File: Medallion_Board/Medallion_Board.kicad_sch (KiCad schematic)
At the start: 3 parts, among them U1 ESP32-S3, U2 MIA-M10Q-00B, U3 ICM-20948

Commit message: Schematic in a good place. IMU, GNSS, LoRa, lipo charging and usb, and neopixels all in.
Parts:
- removed U1: ESP32-S3, Package_DFN_QFN:QFN-56-1EP_7x7mm_P0.4mm_EP4x4mm, symbol MCU_Espressif:ESP32-S3
- removed U2: MIA-M10Q-00B, MIA-M10Q-00B:BGA53C50P9X9_450X450X100, symbol MIA-M10Q-00B:MIA-M10Q-00B
- removed U3: ICM-20948, ICM-20948:QFN40P300X300X105-24N, symbol ICM-20948:ICM-20948
- added C1, C14, C17, C2, C7, C9: 10uF, Capacitor_SMD:C_0805_2012Metric, symbol Adafruit ESP32-S3 8MB No PSRAM-eagle-import:CAP_CERAMIC0805-NOOUTLINE
- added C10, C4, C5: 1uF, Capacitor_SMD:C_0603_1608Metric, symbol Adafruit ESP32-S3 8MB No PSRAM-eagle-import:CAP_CERAMIC0603_NO
- added C11, C6, C8: 10µF, Capacitor_SMD:C_0805_2012Metric, symbol Adafruit ESP32-S3 8MB No PSRAM-eagle-import:CAP_CERAMIC0805-NOOUTLINE
- added C12: 0.1µF, Capacitor_SMD:C_0805_2012Metric, symbol Adafruit ESP32-S3 8MB No PSRAM-eagle-import:CAP_CERAMIC0805-NOOUTLINE
- added C13: 0.1uF, Capacitor_SMD:C_0603_1608Metric, symbol Adafruit ESP32-S3 8MB No PSRAM-eagle-import:CAP_CERAMIC0603_NO
- added C15: 0.1uF, Capacitor_SMD:C_0805_2012Metric, symbol Adafruit ESP32-S3 8MB No PSRAM-eagle-import:CAP_CERAMIC0805-NOOUTLINE
- added C16: 47pF, Capacitor_SMD:C_0805_2012Metric, symbol Adafruit ESP32-S3 8MB No PSRAM-eagle-import:CAP_CERAMIC0805-NOOUTLINE
- added C18: 100nF, Capacitor_SMD:C_0603_1608Metric, symbol Adafruit ESP32-S3 8MB No PSRAM-eagle-import:CAP_CERAMIC0603_NO
- added C3: KW-5R5C104-R, KW-5R5C104-R:CAPPRD500W60D1000H3150, symbol XH414HG-IV01E:XH414HG-IV01E
- added CHG2: ORANGE, LED_SMD:LED_0805_2012Metric, symbol Adafruit ESP32-S3 8MB No PSRAM-eagle-import:LED0603_NOOUTLINE
- added D3: RED, LED_SMD:LED_0603_1608Metric, symbol Adafruit ESP32-S3 8MB No PSRAM-eagle-import:LED0603_NOOUTLINE
- added D4: MBR540, Diode_SMD:D_SOD-123, symbol Adafruit ESP32-S3 8MB No PSRAM-eagle-import:DIODE-SCHOTTKYSOD-123
- added FL1, FL2: BLM15EG121SN1D, BLM15EG121SN1D:BEADC1005X55N, symbol BLM15EG121SN1D:BLM15EG121SN1D
- added J1: RYLR998, Connector_PinHeader_2.54mm:PinHeader_1x05_P2.54mm_Vertical, symbol Connector_Generic:Conn_01x05
- added LED1, LED2, LED3, LED4, LED5, LED6, LED7, LED8, LED9: WS2812B_SK6805_2020, LED_SMD:LED_WS2812B-2020_PLCC4_2.0x2.0mm, symbol Adafruit ESP32-S3 8MB No PSRAM-eagle-import:WS2812B_SK6805_1515
- added Q3: DMG3415U, DMG3415U-7:SOT95P240X105-3N, symbol Adafruit ESP32-S3 8MB No PSRAM-eagle-import:MOSFET-P
- added R1, R10, R11, R13, R6, R9: 5.1K, Resistor_SMD:R_0603_1608Metric, symbol Adafruit ESP32-S3 8MB No PSRAM-eagle-import:RESISTOR_0603_NOOUT
- added R12, R7: 100K, Resistor_SMD:R_0603_1608Metric, symbol Adafruit ESP32-S3 8MB No PSRAM-eagle-import:RESISTOR_0603_NOOUT
- added R17: 1Meg, Resistor_SMD:R_0603_1608Metric, symbol Adafruit ESP32-S3 8MB No PSRAM-eagle-import:RESISTOR_0603_NOOUT
- added R18: 10K, Resistor_SMD:R_0603_1608Metric, symbol Adafruit ESP32-S3 8MB No PSRAM-eagle-import:RESISTOR_0603_NOOUT
- added R3: 10K, Resistor_SMD:R_0603_1608Metric, symbol Adafruit ESP32-S3 8MB No PSRAM-eagle-import:RESISTOR_4PACK
- added R8: 1K, Resistor_SMD:R_0603_1608Metric, symbol Adafruit ESP32-S3 8MB No PSRAM-eagle-import:RESISTOR_0603_NOOUT
- added SW1, SW2: KMR2, Button_Switch_SMD:SW_Push_1P1T-SH_NO_CK_KMR2xxG, symbol Adafruit ESP32-S3 8MB No PSRAM-eagle-import:SWITCH_TACT_SMT4.6X2.8
- added U1: LC86LICMD, LC86LICMD:MODULE_LC86LICMD, symbol LC86LICMD:LC86LICMD
- added U2: AP2112/RT9080-3.3, RT9080-33GJ5:SOT94P280X100-5N, symbol Adafruit ESP32-S3 8MB No PSRAM-eagle-import:VREG_SOT23-5
- added U3: ESP32-S3-MINI-1-N8, ESP32-S3-MINI-1-N8:XCVR_ESP32-S3-MINI-1-N8, symbol ESP32-S3-MINI-1-N8:ESP32-S3-MINI-1-N8
- added U4: BNO085, BNO085:IC_BNO085, symbol BNO085:BNO085
- added U5: MCP73831T-2ACI_OT, MCP73831T-2ACI_OT:SOT95P280X145-5N, symbol MCP73831T-2ACI_OT:MCP73831T-2ACI_OT
- added U6: MAX17048G_T10, MAX17048G_T10:SON50P200X200X80-9N, symbol MAX17048G_T10:MAX17048G_T10
- added X1: JSTPH, Connector_JST:JST_PH_S2B-PH-SM4-TB_1x02-1MP_P2.00mm_Horizontal, symbol Adafruit ESP32-S3 8MB No PSRAM-eagle-import:CON_JST_PH_2PIN_MT_BATT
- added X2: USB4085-GF-A, USB4085-GF-A:GCT_USB4085-GF-A_REVB, symbol USB4085-GF-A:USB4085-GF-A
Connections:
- net GND: now also C1.2, C10.2, C11.2, C12.2, C13.1, C14.2, C15.2, C16.2, C17.2, C18.2, C2.2, C3.2, C4.2, C5.2, C6.2, C7.2, C8.2, C9.2, D3.1, FL2.1, FL2.2, J1.5 (GND), LED1.4 (GND), LED2.4 (GND), LED3.4 (GND), LED4.4 (GND), LED5.4 (GND), LED6.4 (GND), LED7.4 (GND), LED8.4 (GND), LED9.4 (GND), R11.1, R12.1, R13.1, R17.1, R9.1, SW1.1, SW2.1, U1.12 (GND), U1.3 (GND), U2.2 (GND), U3.1 (GND), U3.2 (GND), U3.42 (GND), U3.43 (GND), U3.46 (GND), U3.47 (GND), U3.48 (GND), U3.49 (GND), U3.50 (GND), U3.51 (GND), U3.52 (GND), U3.53 (GND), U3.54 (GND), U3.55 (GND), U3.56 (GND), U3.57 (GND), U3.58 (GND), U3.59 (GND), U3.60 (GND), U3.61 (GND), U3.61_1 (GND), U3.61_2 (GND), U3.61_3 (GND), U3.61_4 (GND), U3.61_5 (GND), U3.61_6 (GND), U3.61_7 (GND), U3.61_8 (GND), U3.62 (GND), U3.63 (GND), U3.64 (GND), U3.65 (GND), U4.2 (GND), U4.25 (GNDIO), U4.5 (PS1), U4.6 (PS0/WAKE), U5.2 (VSS), U6.1 (CTG), U6.4 (GND), U6.6 (QSTRT), U6.9 (EP), X1.1, X2.A1 (GND), X2.A12 (GND), X2.B1 (GND), X2.B12 (GND)
- new net: C18.1, U4.9 (CAP)
- new net: R9.2, U5.5 (PROG)
- new net: R18.1, U4.4 (~{BOOT})
- new net: LED5.3 (DO), LED6.1 (DI)
- new net: LED6.3 (DO), LED7.1 (DI)
- new net: C12.1, U2.4 (P4)
- new net: LED7.3 (DO), LED8.1 (DI)
- new net: LED8.3 (DO), LED9.1 (DI)
- new net: R7.1, U2.3 (EN)
- new net: CHG2.1, R6.1
- new net: R6.2, U5.1 (STAT)
- new net: LED2.3 (DO), LED3.1 (DI)
- new net: LED3.3 (DO), LED4.1 (DI)
- new net: U4.1 (RESV_NC), U4.12 (RESV_NC), U4.13 (RESV_NC), U4.21 (RESV_NC), U4.22 (RESV_NC), U4.23 (RESV_NC), U4.24 (RESV_NC), U4.7 (RESV_NC), U4.8 (RESV_NC)
- new net: C14.1, C15.1, C16.1, FL1.2, J1.1 (VDD)
- new net: R13.2, X2.B5 (CC2)
- new net: D3.2, R10.2
- new net: LED1.3 (DO), LED2.1 (DI)
- new net: R11.2, X2.A5 (CC1)
- new net: C3.1, R8.2, U1.5 (V_BCKP)
- new net: LED4.3 (DO), LED5.1 (DI)
- new net: X2.S1 (SHELL), X2.S2 (SHELL), X2.S3 (SHELL), X2.S4 (SHELL)
- new net +3.3V: C17.1, FL1.1, LED1.2 (VDD), LED2.2 (VDD), LED3.2 (VDD), LED4.2 (VDD), LED5.2 (VDD), LED6.2 (VDD), LED7.2 (VDD), LED8.2 (VDD), LED9.2 (VDD), R3.1 (2), R3.2
- new net 3.3V: C1.1, C10.1, C2.1, C7.1, C8.1, C9.1, R1.2, R18.2, R8.1, U1.4 (VCC), U2.5 (OUT), U3.3 (3V3), U4.28 (VDDIO), U4.3 (VDD)
- new net BNO_NINT: U4.14 (~{H_INT})
- new net BNO_NRST: U4.11 (~{RST})
- new net BOOT0: SW1.2, U3.4 (IO0)
- new net D+: U3.24 (IO20), X2.A6 (DP1)
- new net D-: U3.23 (IO19), X2.B6 (DP2)
- new net D13: R10.1, U3.17 (IO13)
- new net GPS_ANT_ACTIVE: U1.8 (AADET_N), U3.14 (IO10)
- new net GPS_RESET: U1.10 (~{RESET}), U3.13 (IO9)
- new net GPS_WAKEUP: U1.7 (WAKE_UP), U3.12 (IO8)
- new net I2C_PWR: U3.11 (IO7)
- new net IO34_DBLTAP: C5.1, R17.2, U3.29 (IO34)
- new net LORA_NRST: J1.2 (~{RST})
- new net LOW_BATT: U3.9 (IO5), U6.5 (~{ALERT})
- new net NEOPIX: LED1.1 (DI), U3.28 (IO33)
- new net RESET: C4.1, R1.1, SW2.2, U3.45 (EN)
- new net RXD0: U1.2 (TXD), U3.33 (IO37)
- new net RXD1: J1.4 (TXD), U3.35 (IO39)
- new net SCL: R3.1, U3.8 (IO4), U4.19 (H_SCL/SCK/RX), U6.7 (SCL)
- new net SDA: R3.2 (1), U3.7 (IO3), U4.20 (H_SDA/H_MISO/TX), U6.8 (SDA)
- new net TXD0: U1.1 (RXD), U3.32 (IO36)
- new net TXD1: J1.3 (RXD), U3.34 (IO38)
- new net VBAT: C11.1, C13.2, Q3.3 (D), U5.3 (VBAT), U6.2 (CELL), U6.3 (VDD), X1.2
- new net VBUS: CHG2.2, D4.1, Q3.1 (G), R12.2, U5.4 (VDD), X2.A4 (VBUS), X2.A9 (VBUS), X2.B4 (VBUS), X2.B9 (VBUS)
- new net VHI: C6.1, D4.2, Q3.2 (S), R7.2, U2.1 (IN)
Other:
- note added: "1.0K = 1000mA"
- note added: "10K = 100mA"
- note added: "2.0K = 500mA"
- note added: "5.0K = 200mA"
- note added: "Bulk decoupling"
- note added: "CONTROLLER"
- note added: "FUEL GAUGE"
- note added: "GPS"
- note added: "High-frequency filter"
- note added: "I2C SUPPORT"
- note added: "IMU SENSOR"
- note added: "LED"
- note added: "LIPO CHARGING AND REPORTING"
- note added: "LORA RADIO"
- note added: "NEOPIXEL"
- note added: "POWER AND FILTERING"
- note added: "Place as near to ESP32 power rail as possible"
- note added: "USB AND PROGRAMMING BUTTONS"

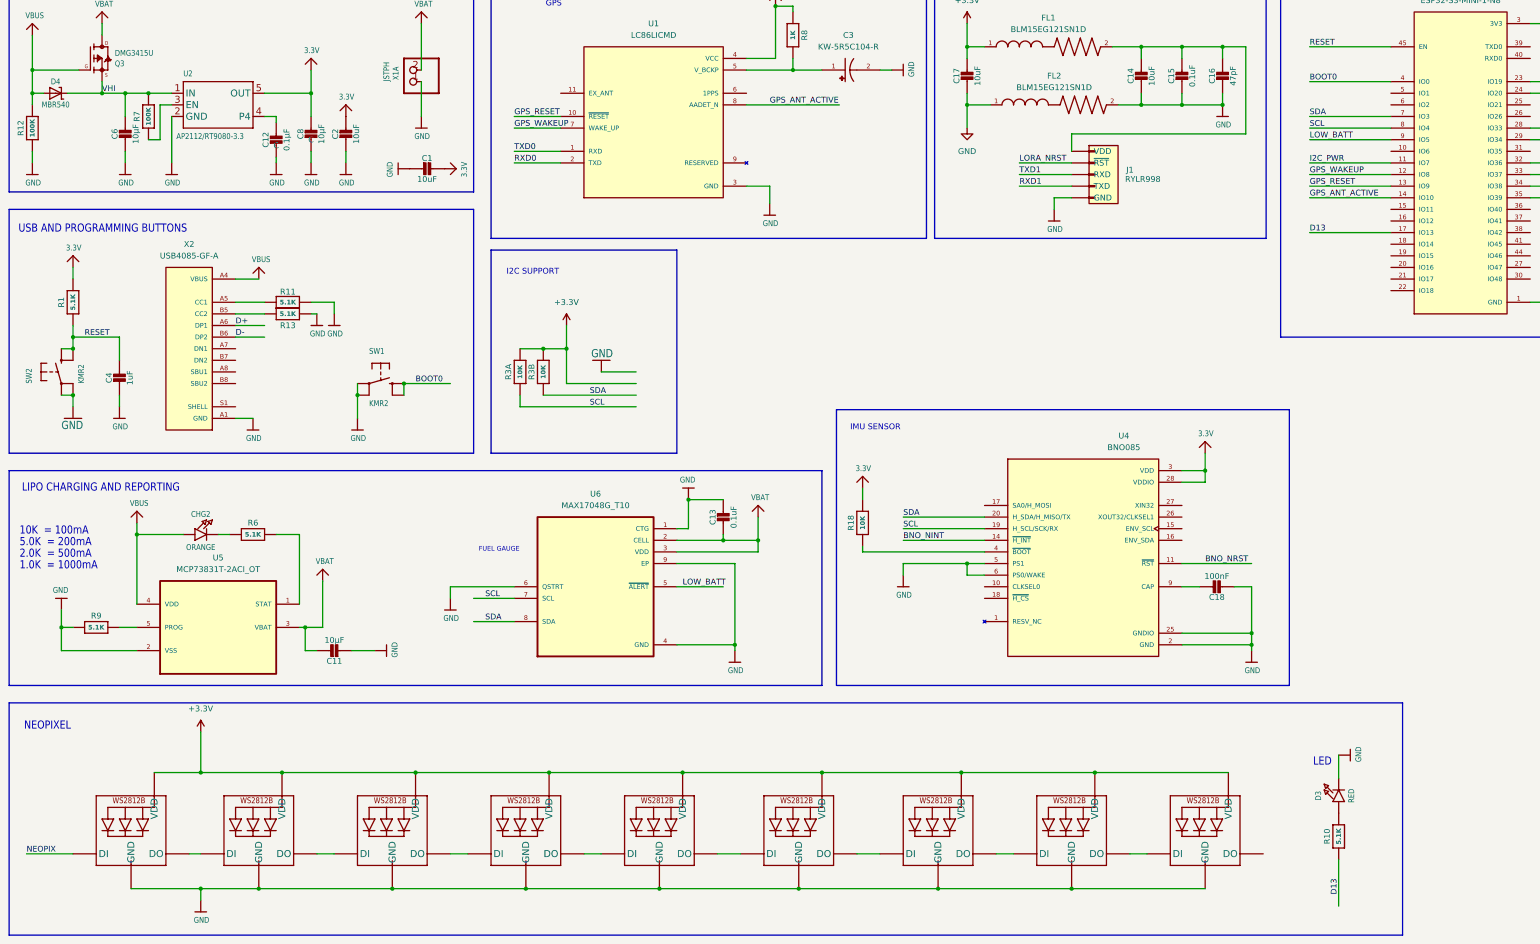
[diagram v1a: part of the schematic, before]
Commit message: Double checked capacitor values and footprints
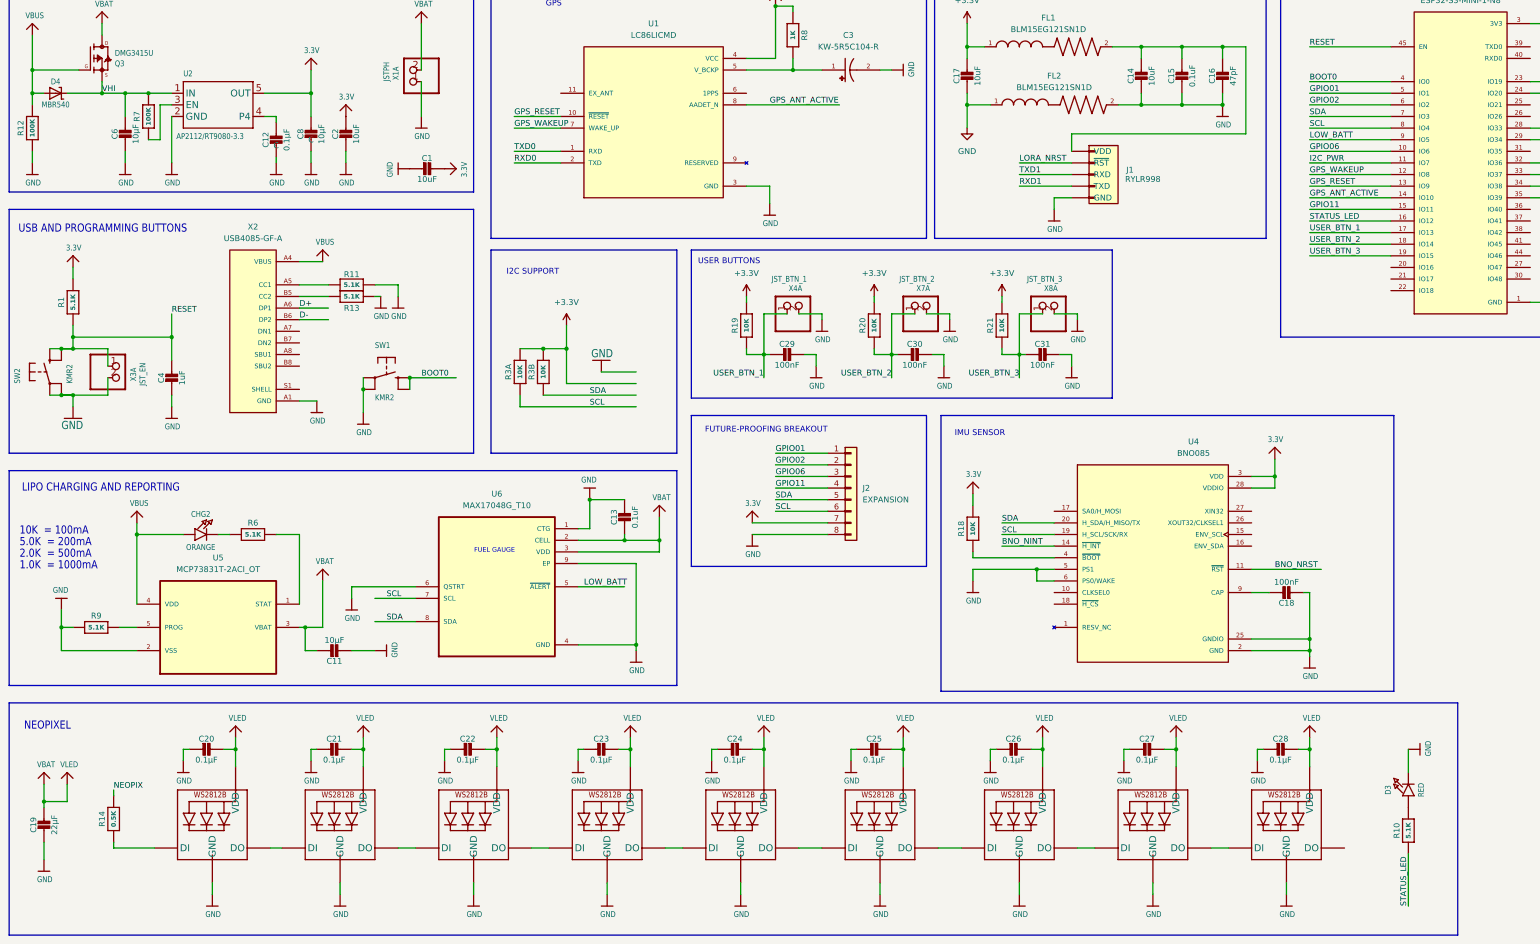
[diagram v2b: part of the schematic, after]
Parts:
- added C19: 22µF, Capacitor_SMD:C_0805_2012Metric, symbol Adafruit ESP32-S3 8MB No PSRAM-eagle-import:CAP_CERAMIC0805-NOOUTLINE
- added C20, C21, C22, C23, C24, C25, C26, C27, C28: 0.1µF, Capacitor_SMD:C_0603_1608Metric, symbol Adafruit ESP32-S3 8MB No PSRAM-eagle-import:CAP_CERAMIC0805-NOOUTLINE
- added C29, C30, C31: 100nF, Capacitor_SMD:C_0603_1608Metric, symbol Adafruit ESP32-S3 8MB No PSRAM-eagle-import:CAP_CERAMIC0603_NO
- added J2: EXPANSION, Connector_PinHeader_2.54mm:PinHeader_1x08_P2.54mm_Vertical, symbol Connector_Generic:Conn_01x08
- added R14: 0.5K, Resistor_SMD:R_0603_1608Metric, symbol Adafruit ESP32-S3 8MB No PSRAM-eagle-import:RESISTOR_0603_NOOUT
- added R19, R20, R21: 10K, Resistor_SMD:R_0603_1608Metric, symbol Adafruit ESP32-S3 8MB No PSRAM-eagle-import:RESISTOR_0603_NOOUT
- added X3: JST_EN, Connector_JST:JST_PH_S2B-PH-SM4-TB_1x02-1MP_P2.00mm_Horizontal, symbol Adafruit ESP32-S3 8MB No PSRAM-eagle-import:CON_JST_PH_2PIN_MT_BATT
- added X4: JST_BTN_1, Connector_JST:JST_PH_S2B-PH-SM4-TB_1x02-1MP_P2.00mm_Horizontal, symbol Adafruit ESP32-S3 8MB No PSRAM-eagle-import:CON_JST_PH_2PIN_MT_BATT
- added X7: JST_BTN_2, Connector_JST:JST_PH_S2B-PH-SM4-TB_1x02-1MP_P2.00mm_Horizontal, symbol Adafruit ESP32-S3 8MB No PSRAM-eagle-import:CON_JST_PH_2PIN_MT_BATT
- added X8: JST_BTN_3, Connector_JST:JST_PH_S2B-PH-SM4-TB_1x02-1MP_P2.00mm_Horizontal, symbol Adafruit ESP32-S3 8MB No PSRAM-eagle-import:CON_JST_PH_2PIN_MT_BATT
- C12, C15, C16: footprint Capacitor_SMD:C_0805_2012Metric -> Capacitor_SMD:C_0402_1005Metric
- C13: footprint Capacitor_SMD:C_0603_1608Metric -> Capacitor_SMD:C_0402_1005Metric
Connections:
- net +3.3V: now also R19.2, R20.2, R21.2; no longer LED1.2 (VDD), LED2.2 (VDD), LED3.2 (VDD), LED4.2 (VDD), LED5.2 (VDD), LED6.2 (VDD), LED7.2 (VDD), LED8.2 (VDD), LED9.2 (VDD)
- net 3.3V: now also J2.7 (Pin_7)
- net GND: now also C19.2, C20.2, C21.2, C22.2, C23.2, C24.2, C25.2, C26.2, C27.2, C28.2, C29.1, C30.1, C31.1, J2.8 (Pin_8), X3.2, X4.2, X7.2, X8.2
- net NEOPIX: now also R14.2; no longer LED1.1 (DI)
- net RESET: now also X3.1
- net SCL: now also J2.6 (Pin_6)
- net SDA: now also J2.5 (Pin_5)
- net VBAT: now also LED1.2 (VDD), LED2.2 (VDD), LED3.2 (VDD), LED4.2 (VDD), LED5.2 (VDD), LED6.2 (VDD), LED7.2 (VDD), LED8.2 (VDD), LED9.2 (VDD), C19.1, C20.1, C21.1, C22.1, C23.1, C24.1, C25.1, C26.1, C27.1, C28.1
- net GPIO06: now reaches U3.10 (IO6)
- net GPIO06: now also J2.3 (Pin_3)
- net GPIO11: now reaches U3.15 (IO11)
- net GPIO11: now also J2.4 (Pin_4)
- net STATUS_LED: now reaches U3.16 (IO12)
- net STATUS_LED: now also R10.1
- net USER_BTN_2: now reaches U3.18 (IO14)
- net USER_BTN_2: now also C30.2, R20.1, X7.1
- net USER_BTN_3: now reaches U3.19 (IO15)
- net USER_BTN_3: now also C31.2, R21.1, X8.1
- net GPIO01: now reaches U3.5 (IO1)
- net GPIO01: now also J2.1 (Pin_1)
- net GPIO02: now reaches U3.6 (IO2)
- net GPIO02: now also J2.2 (Pin_2)
- net D13 renamed USER_BTN_1
- net USER_BTN_1: now also C29.2, R19.1, X4.1; no longer R10.1
- new net: LED1.1 (DI), R14.1
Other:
- note added: "FUTURE-PROOFING BREAKOUT"
- note added: "USER BUTTONS"
- note removed: "LED"
- moved on the sheet: C13, C18, C4, D3, R10, R11, R13, R18, SW1, SW2, U4, U6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

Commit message: More fiddling. Added 3D models to the components
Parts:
- removed C20, C21, C22, C23, C24, C25, C26, C27, C28: 0.1µF, Capacitor_SMD:C_0603_1608Metric, symbol Adafruit ESP32-S3 8MB No PSRAM-eagle-import:CAP_CERAMIC0805-NOOUTLINE
- removed LED1, LED2, LED3, LED4, LED5, LED6, LED7, LED8, LED9: WS2812B_SK6805_2020, LED_SMD:LED_WS2812B-2020_PLCC4_2.0x2.0mm, symbol Adafruit ESP32-S3 8MB No PSRAM-eagle-import:WS2812B_SK6805_1515
- removed R14: 0.5K, Resistor_SMD:R_0603_1608Metric, symbol Adafruit ESP32-S3 8MB No PSRAM-eagle-import:RESISTOR_0603_NOOUT
- removed R3: 10K, Resistor_SMD:R_0603_1608Metric, symbol Adafruit ESP32-S3 8MB No PSRAM-eagle-import:RESISTOR_4PACK
- removed X1: JSTPH, Connector_JST:JST_PH_S2B-PH-SM4-TB_1x02-1MP_P2.00mm_Horizontal, symbol Adafruit ESP32-S3 8MB No PSRAM-eagle-import:CON_JST_PH_2PIN_MT_BATT
- removed X3: JST_EN, Connector_JST:JST_PH_S2B-PH-SM4-TB_1x02-1MP_P2.00mm_Horizontal, symbol Adafruit ESP32-S3 8MB No PSRAM-eagle-import:CON_JST_PH_2PIN_MT_BATT
- removed X4: JST_BTN_1, Connector_JST:JST_PH_S2B-PH-SM4-TB_1x02-1MP_P2.00mm_Horizontal, symbol Adafruit ESP32-S3 8MB No PSRAM-eagle-import:CON_JST_PH_2PIN_MT_BATT
- removed X7: JST_BTN_2, Connector_JST:JST_PH_S2B-PH-SM4-TB_1x02-1MP_P2.00mm_Horizontal, symbol Adafruit ESP32-S3 8MB No PSRAM-eagle-import:CON_JST_PH_2PIN_MT_BATT
- removed X8: JST_BTN_3, Connector_JST:JST_PH_S2B-PH-SM4-TB_1x02-1MP_P2.00mm_Horizontal, symbol Adafruit ESP32-S3 8MB No PSRAM-eagle-import:CON_JST_PH_2PIN_MT_BATT
- added C33, C34, C35, C36, C37, C38, C39, C40, C41: 0.1µF, Capacitor_SMD:C_0603_1608Metric, symbol Adafruit ESP32-S3 8MB No PSRAM-eagle-import:CAP_CERAMIC0805-NOOUTLINE
- added D10, D11, D12, D4, D5, D6, D7, D8, D9: WS2812B2020, WS2812B2020:LED_WS2812B2020, symbol WS2812B2020:WS2812B2020
- added P1: JST_EN, S2B-PH-SM4-TB_LF__SN_:JST_S2B-PH-SM4-TB_LF__SN_, symbol S2B-PH-SM4-TB_LF__SN_:S2B-PH-SM4-TB_LF__SN_
- added P2: JST_PH, S2B-PH-SM4-TB_LF__SN_:JST_S2B-PH-SM4-TB_LF__SN_, symbol S2B-PH-SM4-TB_LF__SN_:S2B-PH-SM4-TB_LF__SN_
- added P3: JST_BTN_1, S2B-PH-SM4-TB_LF__SN_:JST_S2B-PH-SM4-TB_LF__SN_, symbol S2B-PH-SM4-TB_LF__SN_:S2B-PH-SM4-TB_LF__SN_
- added P4: JST_BTN_2, S2B-PH-SM4-TB_LF__SN_:JST_S2B-PH-SM4-TB_LF__SN_, symbol S2B-PH-SM4-TB_LF__SN_:S2B-PH-SM4-TB_LF__SN_
- added P5: JST_BTN_3, S2B-PH-SM4-TB_LF__SN_:JST_S2B-PH-SM4-TB_LF__SN_, symbol S2B-PH-SM4-TB_LF__SN_:S2B-PH-SM4-TB_LF__SN_
- added R10, R9: 10K, Resistor_SMD:R_0603_1608Metric, symbol Adafruit ESP32-S3 8MB No PSRAM-eagle-import:RESISTOR_0603_NOOUT
- added R19: 0.5K, Resistor_SMD:R_0603_1608Metric, symbol Adafruit ESP32-S3 8MB No PSRAM-eagle-import:RESISTOR_0603_NOOUT
- C16: renamed from C3; Availability In Stock -> (none); Check_prices https://www.snapeda.com/parts/XH414HG-IV01E/Seiko/view-part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 -> (none); MPN (none) -> KW-5R5C104-R; PRICE (none) -> 6.63; Package Coin Wide and Corner Terminals Seiko -> (none); Price None -> (none); SnapEDA_Link https://www.snapeda.com/parts/XH414HG-IV01E/Seiko/view-part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 -> (none)
- CHG1: renamed from CHG2; MPN (none) -> LTST-C191KRKT; PRICE (none) -> 0.10
- D1: renamed from D4; value MBR540 -> MBR0540; MPN (none) -> MBR0540; PRICE (none) -> 0.31
- D2: renamed from D3; MPN (none) -> LTST-C191KRKT; PRICE (none) -> 0.10
- FL1, FL2: Availability In Stock -> (none); Check_prices https://www.snapeda.com/parts/BLM15EG121SN1D/Murata/view-pa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 -> (none); MPN (none) -> BLM15EG121SN1D; PRICE (none) -> 0.17; Package 1005 Taiyo Yuden -> (none); Price None -> (none); SnapEDA_Link https://www.snapeda.com/parts/BLM15EG121SN1D/Murata/view-pa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 -> (none)
- J2: renamed from J1; footprint Connector_PinHeader_2.54mm:PinHeader_1x05_P2.54mm_Vertical -> Connector_PinHeader_2.54mm:RYLR998; MPN (none) -> RYLR998; PRICE (none) -> 11.80
- Q1: renamed from Q3; MPN (none) -> DMG3415U-7; PRICE (none) -> 0.48
- R3: renamed from R9; value 5.1K -> 2K
- SW1: renamed from SW2; MPN (none) -> KMR221NG LFS; PRICE (none) -> 0.67
- SW2: renamed from SW1; MPN (none) -> KMR221NG LFS; PRICE (none) -> 0.67
- U1: renamed from U2; value AP2112/RT9080-3.3 -> RT9080-33GJ5; MPN (none) -> RT9080-33GJ5; PRICE (none) -> 0.28
- U2: renamed from U5; Availability In Stock -> (none); Check_prices https://www.snapeda.com/parts/MCP73831T-2ACI/OT/Microchip+T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 -> (none); PRICE (none) -> 0.76; Package SOT-23 Microchip -> (none); Price None -> (none); SnapEDA_Link https://www.snapeda.com/parts/MCP73831T-2ACI/OT/Microchip+T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 -> (none)
- U3: renamed from U6; Availability In Stock -> (none); Check_prices https://www.snapeda.com/parts/MAX17048G+T10/Analog+Devices/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 -> (none); MPN (none) -> MAX17048G+T10; PRICE (none) -> 4.22; Package TDFN-8 Maxim -> (none); Price None -> (none); SnapEDA_Link https://www.snapeda.com/parts/MAX17048G+T10/Analog+Devices/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 -> (none)
- U4: renamed from U1; Availability In Stock -> (none); Check_prices https://www.snapeda.com/parts/LC86LICMD/Quectel/view-part/?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 -> (none); MPN (none) -> LC86LICMD; PRICE (none) -> 12.69; Package Custom Quectel -> (none); Price None -> (none); SnapEDA_Link https://www.snapeda.com/parts/LC86LICMD/Quectel/view-part/?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 -> (none)
- U5: renamed from U4; Availability In Stock -> (none); Check_prices https://www.snapeda.com/parts/BNO085/CEVA+Technologies%252C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 -> (none); MPN (none) -> BNO085; PRICE (none) -> 13.57; Package None -> (none); Price None -> (none); SnapEDA_Link https://www.snapeda.com/parts/BNO085/CEVA+Technologies%252C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 -> (none)
- U6: renamed from U3; Availability In Stock -> (none); Check_prices https://www.snapeda.com/parts/ESP32-S3-MINI-1-N8/Espressif+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 -> (none); MPN (none) -> ESP32-S3-MINI-1-N8; PRICE (none) -> 5.43; Package None -> (none); Price None -> (none); SnapEDA_Link https://www.snapeda.com/parts/ESP32-S3-MINI-1-N8/Espressif+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 -> (none)
- X1: renamed from X2; Availability In Stock -> (none); Check_prices https://www.snapeda.com/parts/USB4085GFA/Global+Connector+T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 -> (none); MPN (none) -> USB4085-GF-A; PRICE None -> 0.91; Package None -> (none); Price None -> (none); SnapEDA_Link https://www.snapeda.com/parts/USB4085GFA/Global+Connector+T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 -> (none)
- renumbered C19 to C1, C1 to C10, C29 to C15, C30 to C18, C17 to C19, C6 to C2, C31 to C21, C14 to C22, C15 to C24, C16 to C25, C18 to C27, C7 to C28, C9 to C29, C4 to C3, C10 to C30, C5 to C31, C12 to C5, C8 to C6, C11 to C8, C2 to C9, J2 to J1, R12 to R1, R19 to R11, R8 to R12, R20 to R13, R18 to R14, R21 to R15, R10 to R16, R1 to R2, R7 to R5, R11 to R7, R13 to R8
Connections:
- net +3.3V: now also R10.2, R9.2
- net GND: now also C33.2, C34.2, C35.2, C36.2, C37.2, C38.2, C39.2, C40.2, C41.2, D10.2 (GND), D11.2 (GND), D12.2 (GND), D4.2 (GND), D5.2 (GND), D6.2 (GND), D7.2 (GND), D8.2 (GND), D9.2 (GND), P1.2, P2.2, P3.2, P4.2, P5.2
- net NEOPIX: now also R19.2
- net RESET: now also P1.1
- net SCL: now also R9.1
- net SDA: now also R10.1
- net USER_BTN_1: now also P3.1
- net USER_BTN_2: now also P4.1
- net USER_BTN_3: now also P5.1
- net VBAT: now also C33.1, C34.1, C35.1, C36.1, C37.1, C38.1, C39.1, C40.1, C41.1, D10.4 (VDD), D11.4 (VDD), D12.4 (VDD), D4.4 (VDD), D5.4 (VDD), D6.4 (VDD), D7.4 (VDD), D8.4 (VDD), D9.4 (VDD), P2.1
- new net: D4.1 (DO), D5.3 (DI)
- new net: D4.3 (DI), R19.1
- new net: D10.1 (DO), D11.3 (DI)
- new net: D10.3 (DI), D9.1 (DO)
- new net: D5.1 (DO), D6.3 (DI)
- new net: D11.1 (DO), D12.3 (DI)
- new net: D8.1 (DO), D9.3 (DI)
- new net: D6.1 (DO), D7.3 (DI)
- new net: D7.1 (DO), D8.3 (DI)
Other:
- note added: "CHARGER"
- moved on the sheet: C3, D2, R16

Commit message: Categorise pcb layout by specsheet boxes
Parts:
- renumbered C28 to C1, C6 to C10, C9 to C11, C5 to C12, C10 to C13, C31 to C14, C18 to C16, C21 to C17, C3 to C18, C13 to C19, C29 to C2, C27 to C20, C8 to C21, C33 to C22, C34 to C23, C35 to C24, C36 to C25, C37 to C26, C38 to C27, C39 to C28, C40 to C29, C30 to C3, C41 to C30, C1 to C31, C16 to C4, C19 to C5, C22 to C6, C24 to C7, C25 to C8, C2 to C9, D11 to D10, D12 to D11, D4 to D3, D5 to D4, D6 to D5, D7 to D6, D8 to D7, D9 to D8, D10 to D9, J2 to J1, J1 to J2, P2 to P1, P3 to P2, P4 to P3, P5 to P4, P1 to P5, R12 to R1, R15 to R10, R9 to R11, R10 to R12, R14 to R13, R6 to R14, R3 to R15, R19 to R17, R5 to R2, R1 to R3, R17 to R4, R7 to R5, R8 to R6, R2 to R7, R11 to R8, R13 to R9, U4 to U2, U6 to U3, U5 to U4, U3 to U5, U2 to U6
